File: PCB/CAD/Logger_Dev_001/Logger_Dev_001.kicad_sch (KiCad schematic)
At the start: 3 parts, among them U2 ESP32-C6-WROOM-1

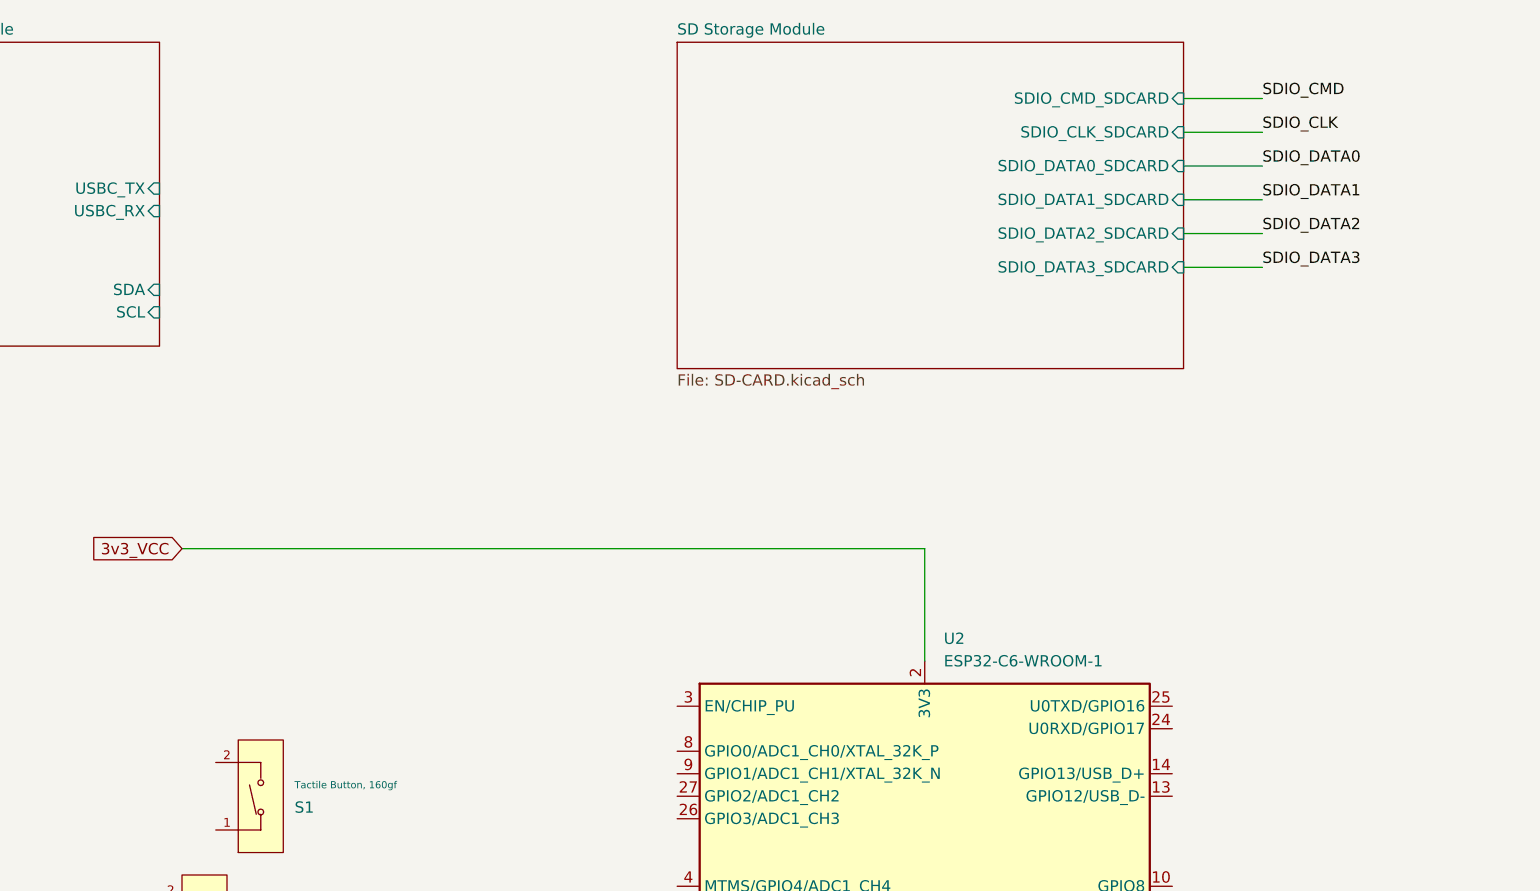
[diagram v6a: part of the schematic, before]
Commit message: Power input Schematic
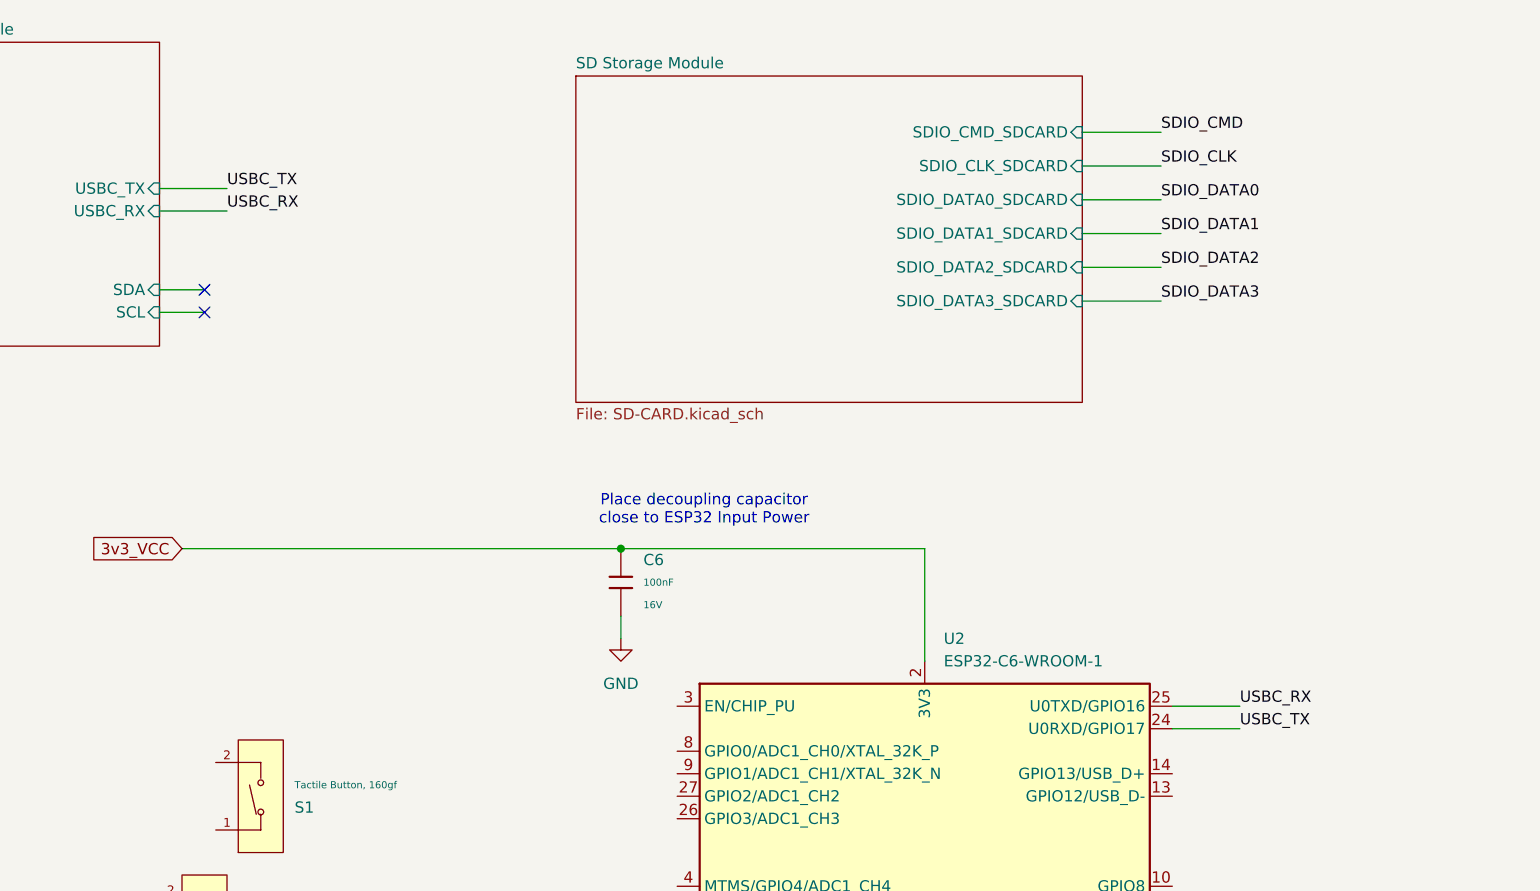
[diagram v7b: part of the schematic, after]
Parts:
- added C6: 100nF, PCM_JLCPCB:C_0402, symbol PCM_JLCPCB-Capacitors:0402,100nF
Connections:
- net 3v3_VCC: now also C6.1
- net GND: now also C6.2
- net USBC_TX: now reaches U2.24 (U0RXD/GPIO17)
- net USBC_RX: now reaches U2.25 (U0TXD/GPIO16)
- no-connect marks 0 -> 2
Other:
- note added: "Place decoupling capacitor close to ESP32 Input Power"

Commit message: Updated Schematic
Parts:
- added C10, C11, C12, C13: 100nF, PCM_JLCPCB:C_0402, symbol PCM_JLCPCB-Capacitors:0402,100nF
- added R15, R16: 10kΩ, PCM_JLCPCB:R_0402, symbol PCM_JLCPCB-Resistors:0402,10kΩ
- added S3: Tactile Button, 160gf, PCM_JLCPCB:SW_TS-1088-AR02016, symbol PCM_JLCPCB-Connectors_Buttons:Tactile Button, 160gf, 12V, 50mA, 4.0mm
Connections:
- net 3v3_VCC: now also R15.1, R16.1
- net GND: now also S1.1 (A), S2.1 (A), C10.2, C11.2, C12.2, C13.2, S3.1 (A)
- net BTN_FUNCTION: now reaches U2.11 (GPIO10)
- net BTN_FUNCTION: now also C13.1, R16.2, S3.2 (B)
- net GPIO9_BOOT: now reaches U2.15 (GPIO9)
- net GPIO9_BOOT: now also S1.2 (B), C12.1
- net EN: now reaches U2.3 (EN/CHIP_PU)
- net EN: now also S2.2 (B), C10.1, C11.1, R15.2
- net GPS_TX: now reaches U2.4 (MTMS/GPIO4/ADC1_CH4)
- net GPS_RX: now reaches U2.5 (MTDI/GPIO5/ADC1_CH5)
- no-connect marks 2 -> 0
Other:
- sheet USB C to 3v3 Power Input Module renamed USB C COMs 3v3 Power Input Module
- sheet GPS Module ports: added !GPS_RX, !GPS_TX; removed none
- sheet SD Storage Module ports: added !SDIO_CLK_SDCARD, !SDIO_CMD_SDCARD, !SDIO_DATA0_SDCARD, !SDIO_DATA1_SDCARD, !SDIO_DATA2_SDCARD, !SDIO_DATA3_SDCARD; removed SDIO_CLK_SDCARD, SDIO_CMD_SDCARD, SDIO_DATA0_SDCARD, SDIO_DATA1_SDCARD, SDIO_DATA2_SDCARD, SDIO_DATA3_SDCARD
- sheet USB C COMs 3v3 Power Input Module ports: added !EN, !GPIO9_BOOT, !USBC_RX, !USBC_TX; removed SCL, SDA, USBC_RX, USBC_TX
- company: (none) -> Jake Odgers
- title: (none) -> Mileage Logger
- moved on the sheet: C6, S1, S2, U2
